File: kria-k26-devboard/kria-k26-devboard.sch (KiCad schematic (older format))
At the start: 0 parts

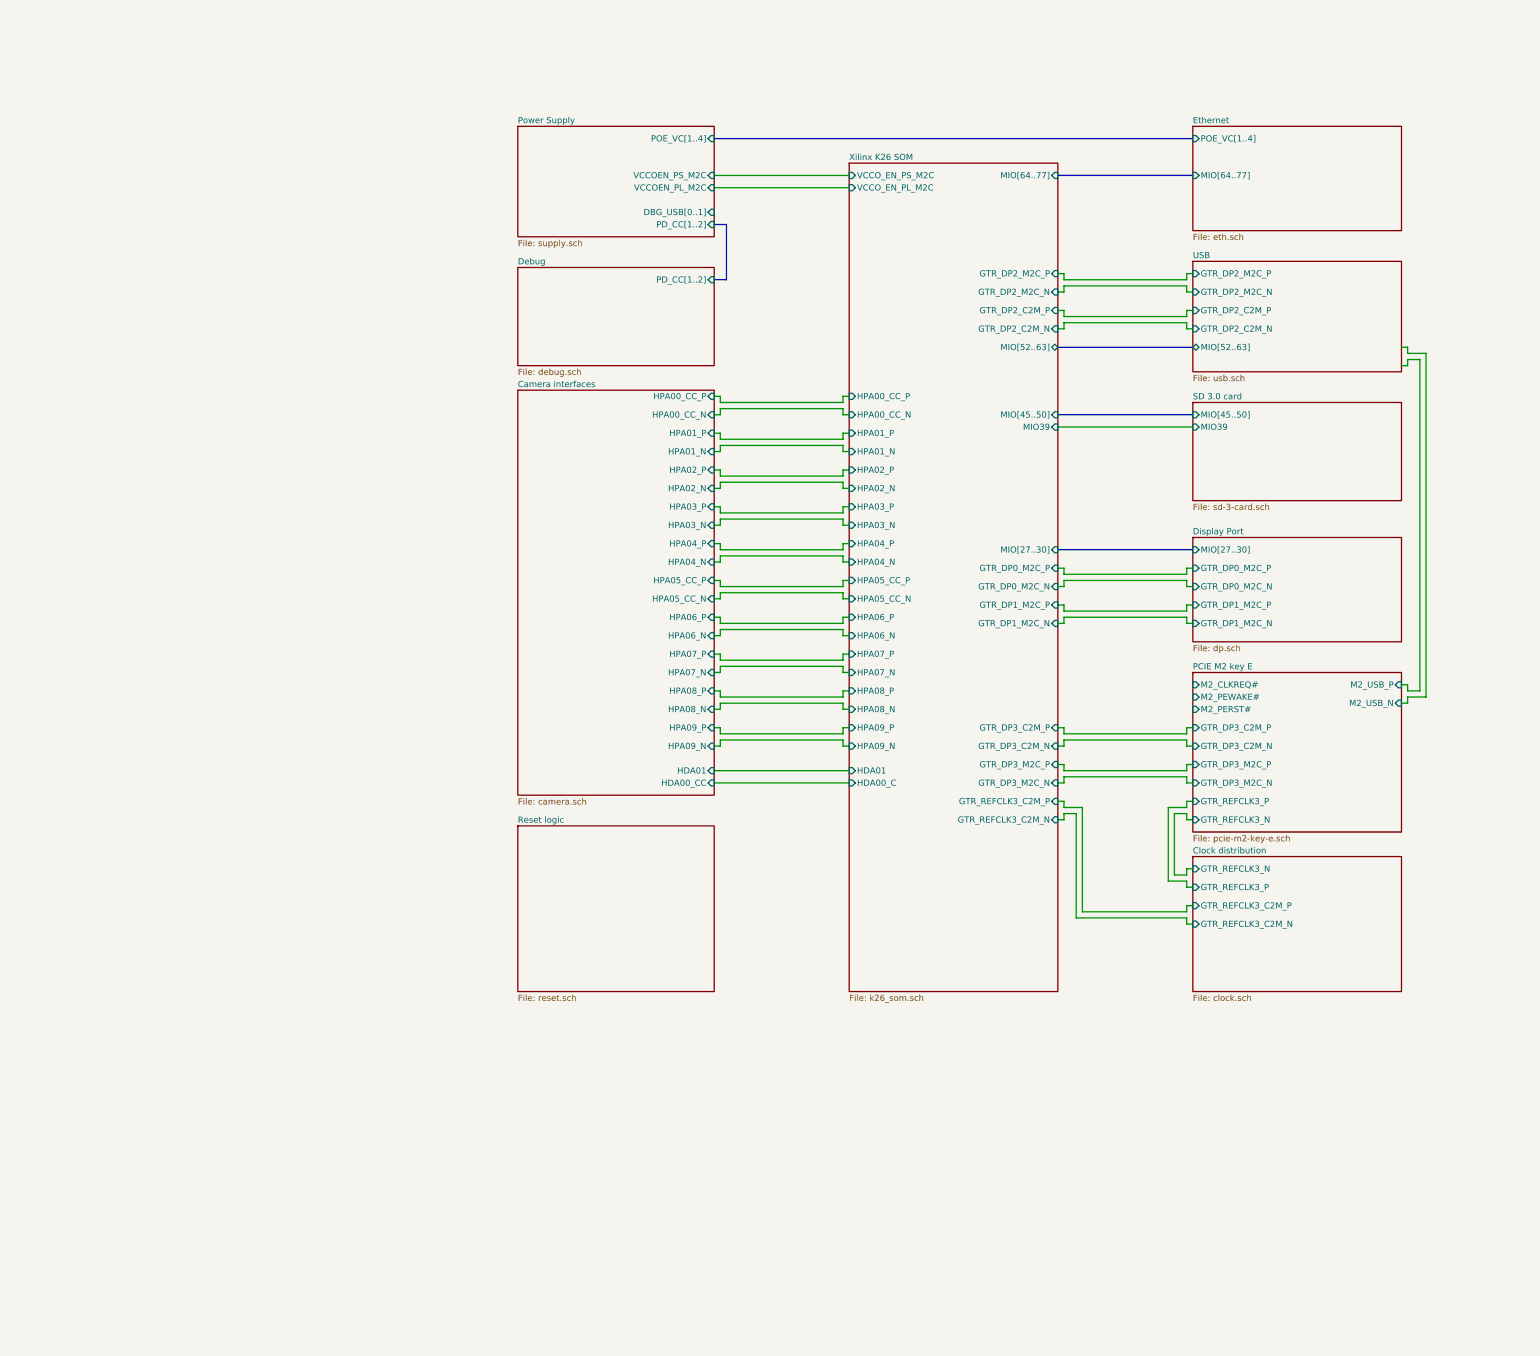
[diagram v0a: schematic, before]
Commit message: Finished reset logic, added crystal gen. to USB PHY, create power toggle for SD 3.0
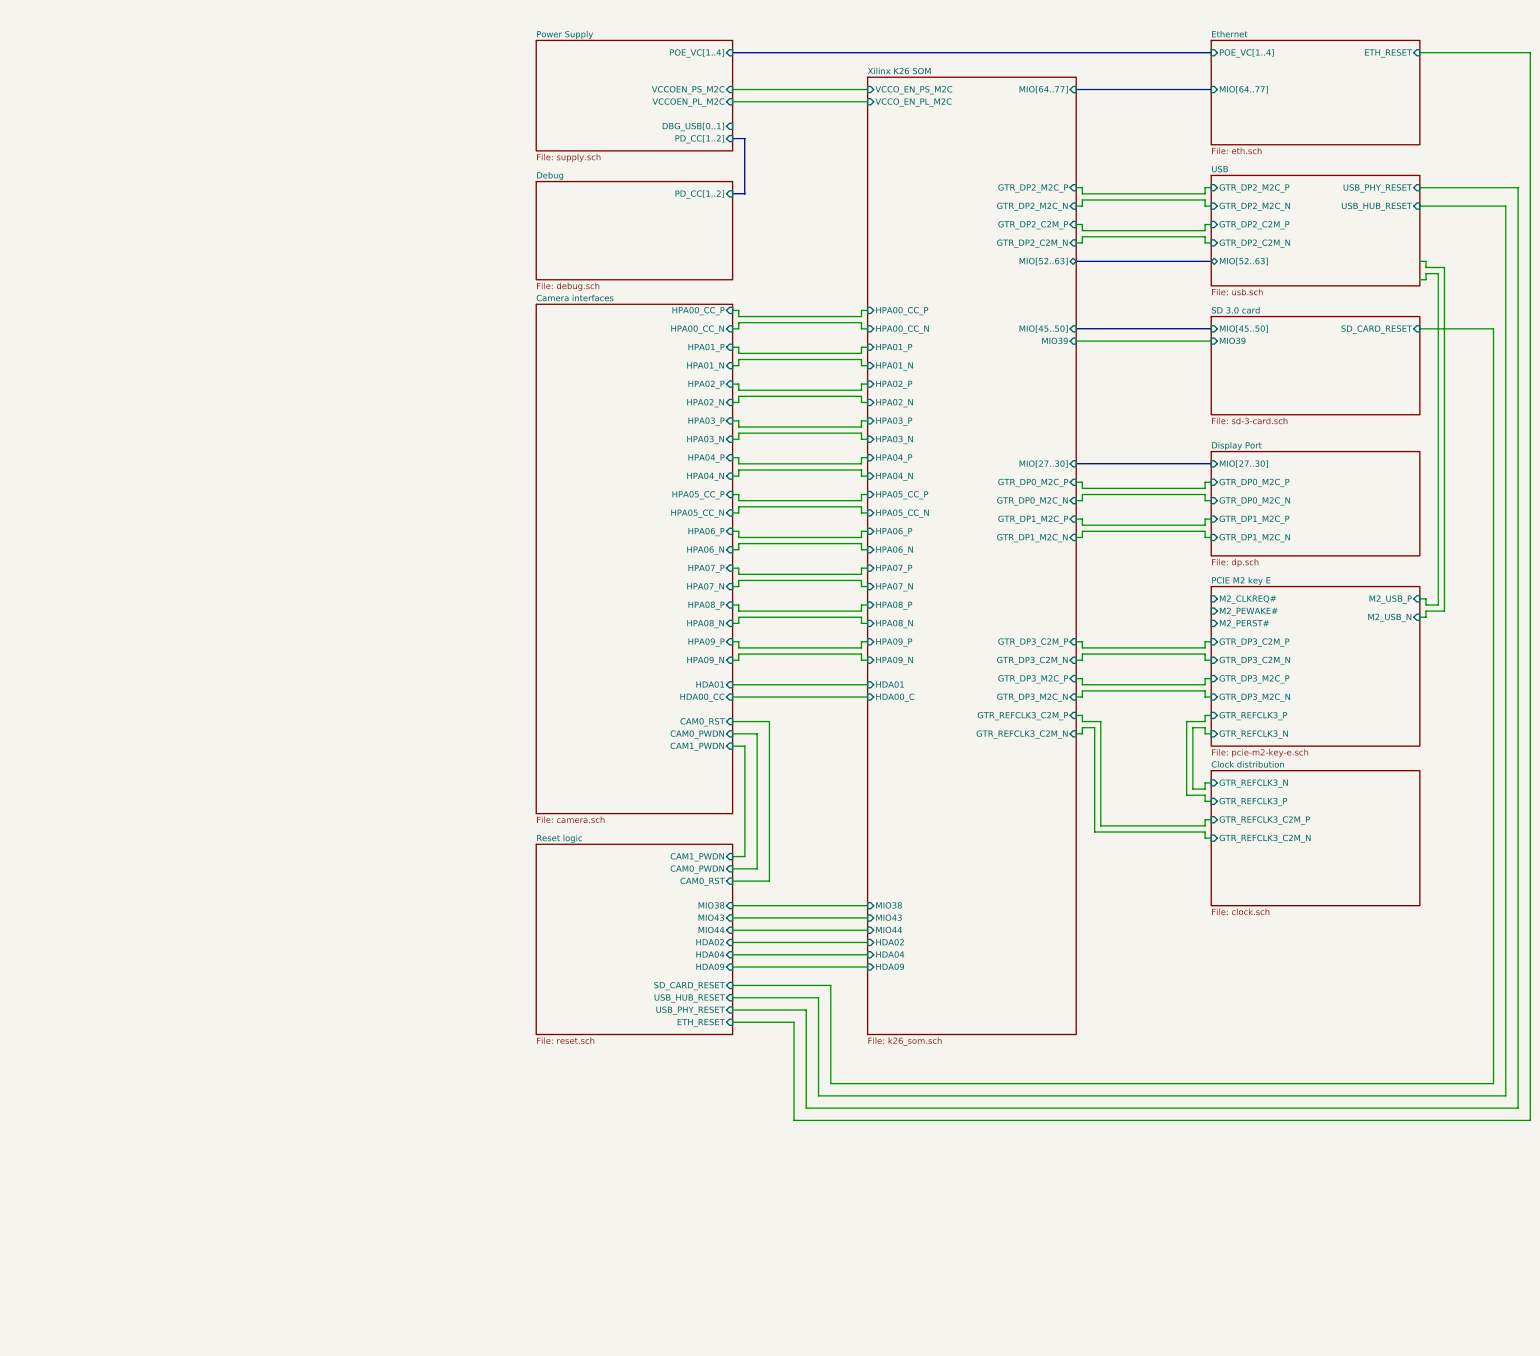
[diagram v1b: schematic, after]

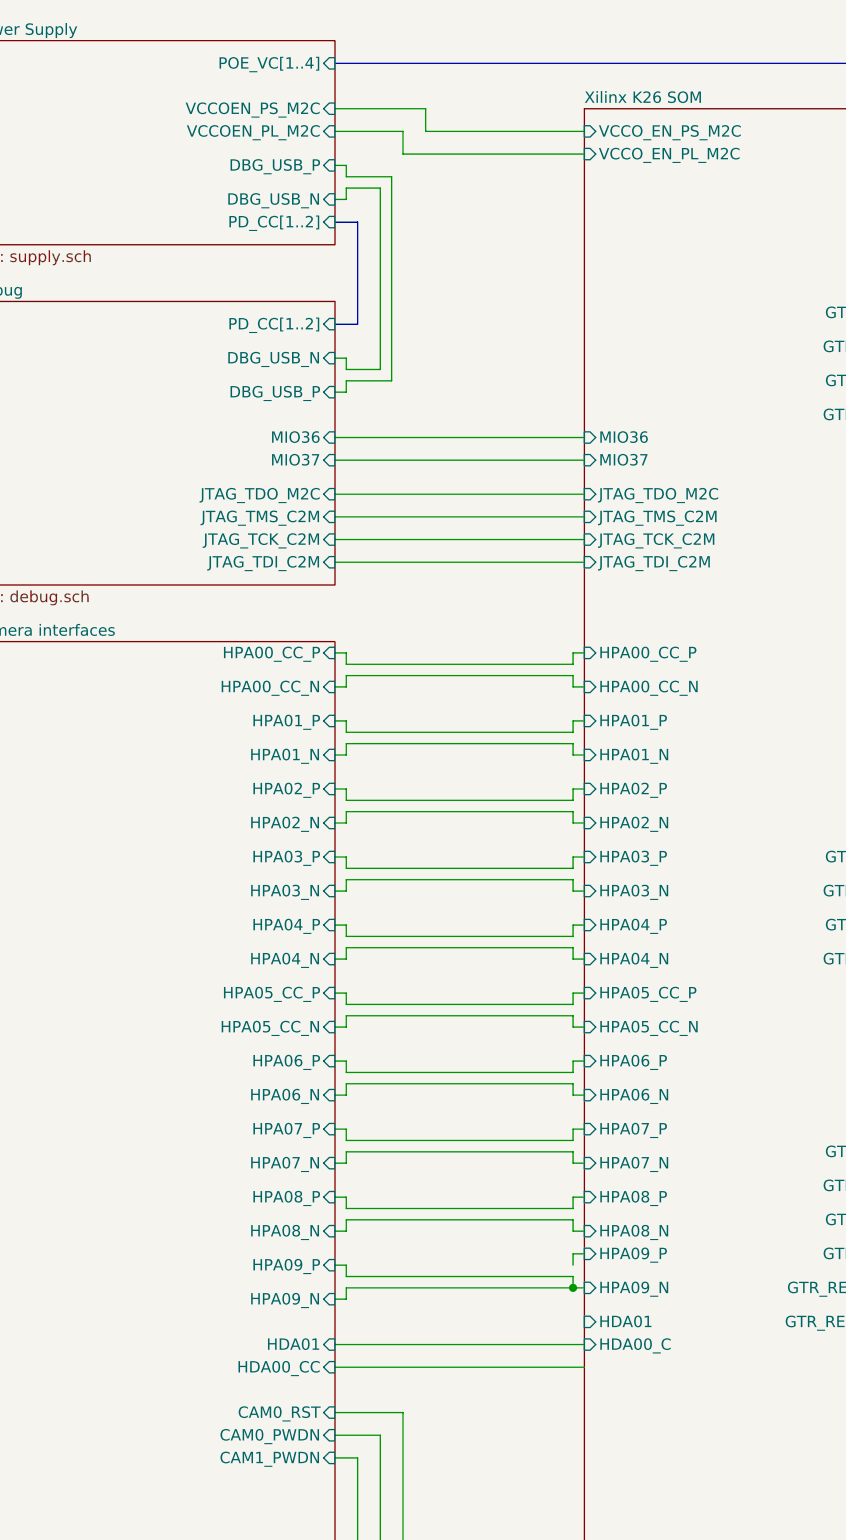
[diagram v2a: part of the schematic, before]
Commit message: Finished Debug and JTAG schematic
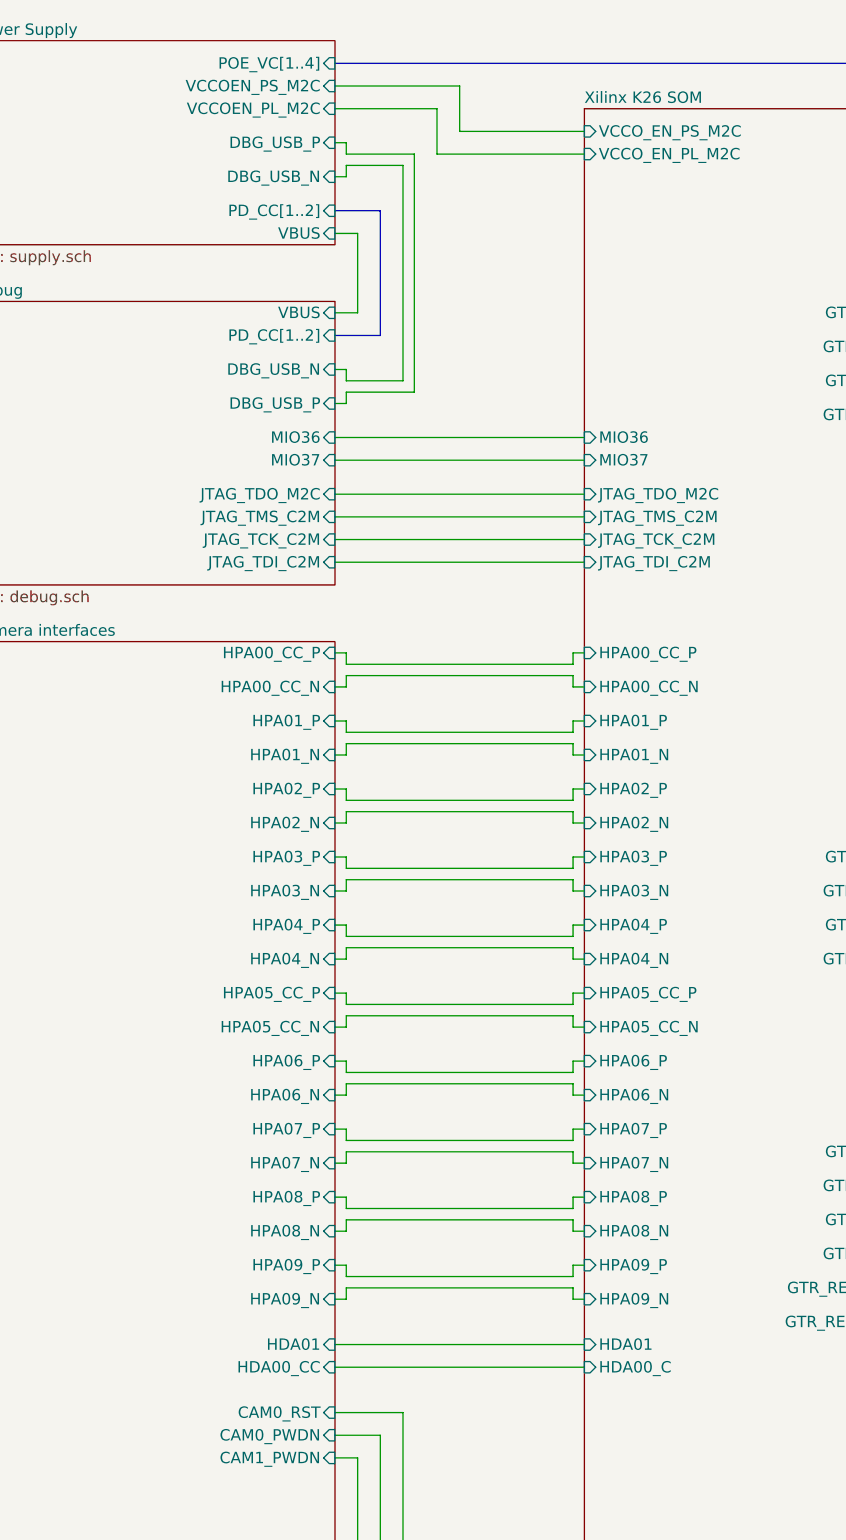
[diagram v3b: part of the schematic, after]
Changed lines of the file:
@@
 F0 "Power Supply" 50
 F1 "supply.sch" 50
-F2 "PD_CC[1..2]" I R 5950 1600 50
-F3 "VCCOEN_PS_M2C" I R 5950 1100 50
-F4 "VCCOEN_PL_M2C" I R 5950 1200 50
+F2 "PD_CC[1..2]" I R 5950 1550 50
+F3 "VCCOEN_PS_M2C" I R 5950 1000 50
+F4 "VCCOEN_PL_M2C" I R 5950 1100 50
 F5 "POE_VC[1..4]" I R 5950 900 50
-F6 "DBG_USB_P" I R 5950 1350 50
-F7 "DBG_USB_N" I R 5950 1500 50
+F6 "DBG_USB_P" I R 5950 1250 50
+F7 "DBG_USB_N" I R 5950 1400 50
+F8 "VBUS" I R 5950 1650 50
 $EndSheet
 $Sheet
@@
 F0 "Debug" 50
 F1 "debug.sch" 50
-F2 "PD_CC[1..2]" I R 5950 2050 50
+F2 "PD_CC[1..2]" I R 5950 2100 50
 F3 "JTAG_TDO_M2C" I R 5950 2800 50
 F4 "JTAG_TMS_C2M" I R 5950 2900 50
 F5 "JTAG_TCK_C2M" I R 5950 3000 50
 F6 "JTAG_TDI_C2M" I R 5950 3100 50
-F7 "DBG_USB_P" I R 5950 2350 50
-F8 "DBG_USB_N" I R 5950 2200 50
+F7 "DBG_USB_P" I R 5950 2400 50
+F8 "DBG_USB_N" I R 5950 2250 50
 F9 "MIO37" I R 5950 2650 50
 F10 "MIO36" I R 5950 2550 50
-$EndSheet
-Wire Bus Line
-	6050 2050 5950 2050
+F11 "VBUS" I R 5950 2000 50
+$EndSheet
 Wire Bus Line
 	5950 900  9850 900
 Wire Wire Line
-	5950 1200 6250 1200
-Wire Bus Line
-	6050 1600 5950 1600
-Wire Bus Line
-	6050 1600 6050 2050
+	5950 1100 6400 1100
 $Sheet
 S 9850 5250 1700 1300
@@
 F31 "HPA01_P" I L 7050 3800 50
 F32 "HPA01_N" I L 7050 3950 50
-F33 "HPA09_P" I L 7050 6150 50
-F34 "HPA09_N" I L 7050 6300 50
+F33 "HPA09_P" I L 7050 6200 50
+F34 "HPA09_N" I L 7050 6350 50
 F35 "HPA05_CC_P" I L 7050 5000 50
 F36 "HPA05_CC_N" I L 7050 5150 50
@@
 F41 "HPA07_P" I L 7050 5600 50
 F42 "HPA07_N" I L 7050 5750 50
-F43 "HDA00_C" I L 7050 6550 50
-F44 "HDA01" I L 7050 6450 50
+F43 "HDA00_C" I L 7050 6650 50
+F44 "HDA01" I L 7050 6550 50
 F45 "MIO38" I L 7050 8350 50
 F46 "MIO44" I L 7050 8550 50
@@
 	7000 6050 7050 6050
 Wire Wire Line
-	7000 6200 7000 6150
-Wire Wire Line
-	7000 6150 7050 6150
-Wire Wire Line
-	7000 6250 7000 6300
-Wire Wire Line
-	7000 6300 7050 6300
+	7000 6250 7000 6200
+Wire Wire Line
+	7000 6200 7050 6200
+Wire Wire Line
+	7000 6300 7000 6350
+Wire Wire Line
+	7000 6350 7050 6350
 Wire Wire Line
 	8800 6400 8900 6400
@@
 	12450 900  11550 900
 Wire Wire Line
-	5950 2200 6000 2200
-Wire Wire Line
-	6000 2200 6000 2250
-Wire Wire Line
-	6150 1450 6000 1450
-Wire Wire Line
-	6000 1450 6000 1500
-Wire Wire Line
-	6000 1500 5950 1500
-Wire Wire Line
-	6000 2250 6150 2250
-Wire Wire Line
-	5950 1100 6350 1100
-Wire Wire Line
-	6350 1100 6350 1200
-Wire Wire Line
-	6350 1200 7050 1200
-Wire Wire Line
-	6250 1300 6250 1200
-Wire Wire Line
-	6250 1300 7050 1300
-Wire Wire Line
-	5950 1350 6000 1350
+	5950 2250 6000 2250
+Wire Wire Line
+	6000 2250 6000 2300
+Wire Wire Line
+	6250 1350 6000 1350
 Wire Wire Line
 	6000 1350 6000 1400
 Wire Wire Line
-	6000 1400 6200 1400
-Wire Wire Line
-	6200 2300 6000 2300
-Wire Wire Line
-	6000 2300 6000 2350
-Wire Wire Line
-	6000 2350 5950 2350
-Wire Wire Line
-	6150 1450 6150 2250
-Wire Wire Line
-	6200 1400 6200 2300
+	6000 1400 5950 1400
+Wire Wire Line
+	6000 2300 6250 2300
+Wire Wire Line
+	5950 1000 6500 1000
+Wire Wire Line
+	6500 1200 7050 1200
+Wire Wire Line
+	6400 1300 7050 1300
+Wire Wire Line
+	5950 1250 6000 1250
+Wire Wire Line
+	6000 1250 6000 1300
+Wire Wire Line
+	6000 1300 6300 1300
+Wire Wire Line
+	6300 2350 6000 2350
+Wire Wire Line
+	6000 2350 6000 2400
+Wire Wire Line
+	6000 2400 5950 2400
 $Sheet
 S 4350 3450 1600 4150
@@
 	6000 6200 6000 6250
 Wire Wire Line
-	6000 6250 7000 6250
-Wire Wire Line
 	5950 6350 6000 6350
 Wire Wire Line
 	6000 6350 6000 6300
-Wire Wire Line
-	6000 6300 7000 6300
 Wire Wire Line
 	5950 6550 7050 6550
@@
 Wire Wire Line
 	6450 9300 6450 9800
-Connection ~ 7000 6300
 Wire Wire Line
 	5950 2550 7050 2550
@@
 Wire Wire Line
 	5950 3100 7050 3100
+Wire Wire Line
+	6000 6250 7000 6250
+Wire Wire Line
+	7000 6300 6000 6300
+Wire Wire Line
+	6500 1000 6500 1200
+Wire Wire Line
+	6400 1100 6400 1300
+Wire Bus Line
+	6150 1550 5950 1550
+Wire Wire Line
+	6250 1350 6250 2300
+Wire Wire Line
+	6300 1300 6300 2350
+Wire Wire Line
+	5950 2000 6050 2000
+Wire Wire Line
+	6050 2000 6050 1650
+Wire Wire Line
+	6050 1650 5950 1650
+Wire Bus Line
+	5950 2100 6150 2100
+Wire Bus Line
+	6150 1550 6150 2100
 $EndSCHEMATC

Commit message: Added finished i2c (wirh eeprom) and pmod sheet. Added JTAG connector with collision avoidance logic
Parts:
- added N?: oshw_logo, antmicro-footprints:oshw-logo, symbol antmicroMechanicalParts:oshw_logo
- added N?: antmicro_logo, antmicro-footprints:antmicro-logo, symbol antmicroMechanicalParts:antmicro_logo
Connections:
- wire segments 269 -> 283
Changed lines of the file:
@@
 $Descr A3 16535 11693
 encoding utf-8
-Sheet 1 17
+Sheet 1 19
 Title "Kria K26 Devboard"
 Date "2022-03-10"
@@
 S 4350 1950 1600 1250
 U 625B0244
-F0 "Debug" 50
+F0 "Debug and JTAG" 50
 F1 "debug.sch" 50
 F2 "PD_CC[1..2]" I R 5950 2100 50
-F3 "JTAG_TDO_M2C" I R 5950 2800 50
-F4 "JTAG_TMS_C2M" I R 5950 2900 50
-F5 "JTAG_TCK_C2M" I R 5950 3000 50
-F6 "JTAG_TDI_C2M" I R 5950 3100 50
+F3 "JTAG_TDO_M2C" I R 5950 2750 50
+F4 "JTAG_TMS_C2M" I R 5950 2850 50
+F5 "JTAG_TCK_C2M" I R 5950 2950 50
+F6 "JTAG_TDI_C2M" I R 5950 3050 50
 F7 "DBG_USB_P" I R 5950 2400 50
 F8 "DBG_USB_N" I R 5950 2250 50
@@
 F10 "MIO36" I R 5950 2550 50
 F11 "VBUS" I R 5950 2000 50
+F12 "EEPROM_WC" I L 4350 3050 50
+F13 "~PS_POR" I L 4350 3150 50
 $EndSheet
 Wire Bus Line
@@
 F51 "MIO36" I L 7050 2550 50
 F52 "MIO37" I L 7050 2650 50
-F53 "JTAG_TMS_C2M" I L 7050 2900 50
-F54 "JTAG_TDO_M2C" I L 7050 2800 50
-F55 "JTAG_TDI_C2M" I L 7050 3100 50
-F56 "JTAG_TCK_C2M" I L 7050 3000 50
+F53 "JTAG_TMS_C2M" I L 7050 2850 50
+F54 "JTAG_TDO_M2C" I L 7050 2750 50
+F55 "JTAG_TDI_C2M" I L 7050 3050 50
+F56 "JTAG_TCK_C2M" I L 7050 2950 50
+F57 "MIO24_I2C_SCK" I R 8750 8150 50
+F58 "MIO25_I2C_SDA" I R 8750 8250 50
+F59 "HDA[11..18]" I R 8750 8800 50
+F60 "HDA16_CC" I R 8750 8900 50
+F61 "~PS_POR" I L 7050 8250 50
 $EndSheet
 Wire Wire Line
@@
 F13 "HDA04" I R 5950 8750 50
 F14 "HDA09" I R 5950 8850 50
+F15 "~PS_POR" I R 5950 8250 50
 $EndSheet
 Wire Wire Line
@@
 Wire Wire Line
 	6450 9300 6450 9800
-Wire Wire Line
-	5950 2550 7050 2550
-Wire Wire Line
-	7050 2650 5950 2650
-Wire Wire Line
-	5950 2800 7050 2800
-Wire Wire Line
-	7050 2900 5950 2900
-Wire Wire Line
-	7050 3000 5950 3000
-Wire Wire Line
-	5950 3100 7050 3100
 Wire Wire Line
 	6000 6250 7000 6250
@@
 Wire Bus Line
 	6150 1550 6150 2100
+$Sheet
+S 9850 8050 1700 450
+U 63AA2BFE
+F0 "I2C " 50
+F1 "i2c.sch" 50
+F2 "MIO24_I2C_SCK" I L 9850 8150 50
+F3 "MIO24_I2C_SDA" I L 9850 8250 50
+F4 "I2C_SDA_3V3" I R 11550 8250 50
+F5 "I2C_SCK_3V3" I R 11550 8150 50
+F6 "EEPROM_WC_B" I R 11550 8400 50
+$EndSheet
+Wire Wire Line
+	11650 10150 3950 10150
+Wire Wire Line
+	3950 3050 4350 3050
+Wire Wire Line
+	8750 8150 9850 8150
+Wire Wire Line
+	9850 8250 8750 8250
+Wire Wire Line
+	11650 8400 11550 8400
+Wire Wire Line
+	11650 8400 11650 10150
+$Comp
+L antmicroMechanicalParts:oshw_logo N?
+U 1 1 63FCC534
+P 700 11000
+F 0 "N?" H 894 11003 50  0000 L CNN
+F 1 "oshw_logo" H 894 10912 50  0000 L CNN
+F 2 "antmicro-footprints:oshw-logo" H 720 10760 50  0001 C CNN
+F 3 "" H 700 11000 50  0001 C CNN
+	1    700  11000
+	1    0    0    -1
+$EndComp
+$Comp
+L antmicroMechanicalParts:antmicro_logo N?
+U 1 1 63FCC88F
+P 650 10850
+F 0 "N?" H 864 10943 50  0000 L CNN
+F 1 "antmicro_logo" H 864 10852 50  0000 L CNN
+F 2 "antmicro-footprints:antmicro-logo" H 550 11100 50  0001 C CNN
+F 3 "" H 650 11200 50  0001 C CNN
+	1    650  10850
+	1    0    0    -1
+$EndComp
+$Sheet
+S 9850 8700 1700 650
+U 63FE614F
+F0 "PMOD" 50
+F1 "pmod.sch" 50
+F2 "HDA[11..18]" I L 9850 8800 50
+F3 "HDA16_CC" I L 9850 8900 50
+$EndSheet
+Wire Bus Line
+	8750 8800 9850 8800
+Wire Wire Line
+	8750 8900 9850 8900
+Wire Wire Line
+	5950 3050 7050 3050
+Wire Wire Line
+	7050 2950 5950 2950
+Wire Wire Line
+	7050 2850 5950 2850
+Wire Wire Line
+	5950 2750 7050 2750
+Wire Wire Line
+	7050 2650 5950 2650
+Wire Wire Line
+	5950 2550 7050 2550
+Wire Wire Line
+	3950 3050 3950 10150
+Wire Wire Line
+	5950 8250 6350 8250
+Wire Wire Line
+	4350 3150 4250 3150
+Wire Wire Line
+	4250 3150 4250 7750
+Wire Wire Line
+	4250 7750 6350 7750
+Wire Wire Line
+	6350 7750 6350 8250
+Connection ~ 6350 8250
+Wire Wire Line
+	6350 8250 7050 8250
 $EndSCHEMATC
